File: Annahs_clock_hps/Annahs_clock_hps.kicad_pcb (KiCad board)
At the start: 2 copper layers, 140 x 90 mm, 44 parts, among them J1 Conn_01x06, J2 Power_inlet_vertical, SW1 Omron_B3F_SPST, SW2 Omron_B3F_SPST, SW3 Omron_B3F_SPST, SW4 Omron_B3F_SPST, SW5 Omron_B3F_SPST, U1 DS1307_DIP-8, U2 MAX7219, U3 L7805, U4 SC56-11EWA, U5 SC56-11EWA, Y1 Crystal_16MHz, Y2 Crystal_32768Hz

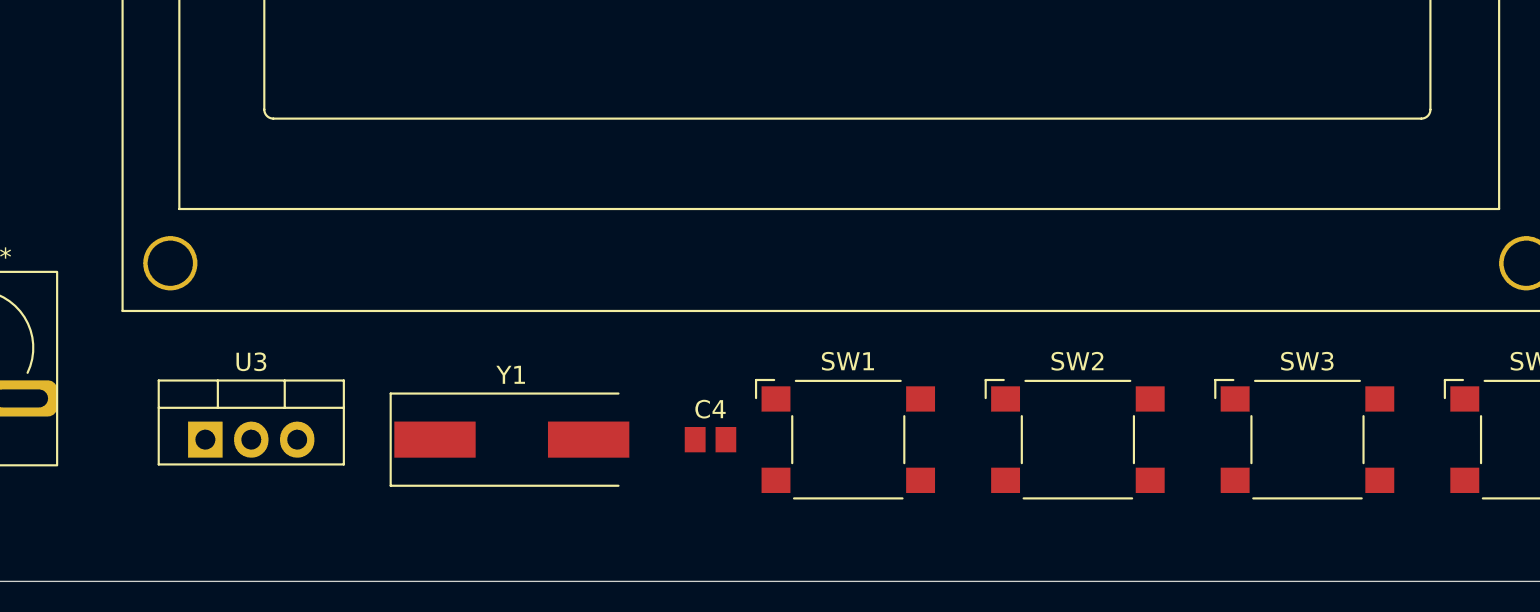
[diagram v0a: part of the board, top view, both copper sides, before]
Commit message: Updated Footprint Schematic and PCB
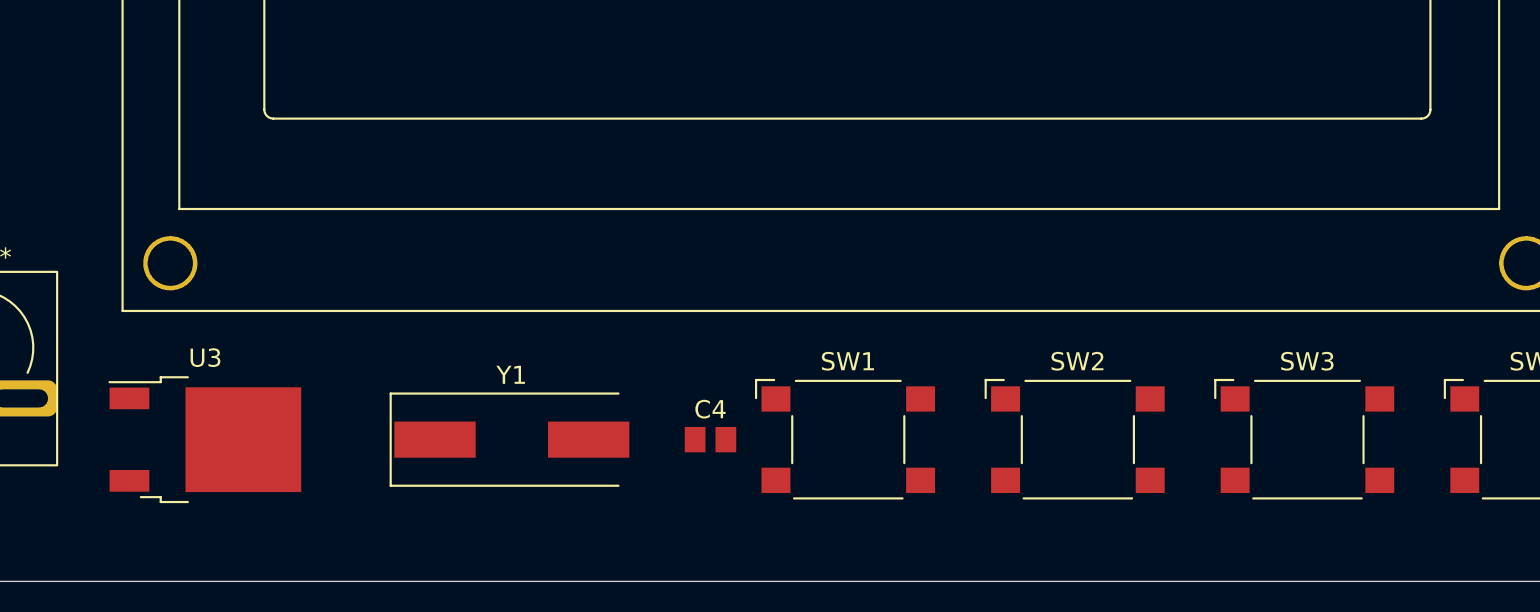
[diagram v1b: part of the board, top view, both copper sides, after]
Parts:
- U3: footprint footprints:TO-220-3_Vertical -> footprints:TO-252-2
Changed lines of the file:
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@@
     )
   )
-  (footprint "footprints:TO-220-3_Vertical" (layer "F.Cu")
+  (footprint "footprints:TO-252-2" (layer "F.Cu")
     (at 114.3 137.16)
-    (descr "TO-220-3, Vertical, RM 2.54mm, see https://www.vishay.com/docs/66542/to-220-1.pdf")
-    (tags "TO-220-3 Vertical RM 2.54mm")
-    (property "Sheetfile" "Annahs_clock_hps.kicad_sch")
-    (property "Sheetname" "")
-    (attr smd)
-    (fp_text reference "U3" (at 2.54 -4.27) (layer "F.SilkS")
-      (effects (font (size 1 1) (thickness 0.15)))
-    )
-    (fp_text value "L7805" (at 2.54 2.5) (layer "F.Fab")
-      (effects (font (size 1 1) (thickness 0.15)))
-    )
-    (fp_text user "${REFERENCE}" (at 2.54 -4.27) (layer "F.Fab")
-      (effects (font (size 1 1) (thickness 0.15)))
-    )
-    (fp_line (start -2.58 -1.76) (end 7.66 -1.76) (layer "F.SilkS") (width 0.12))
-    (fp_line (start 4.391 -3.27) (end 4.391 -1.76) (layer "F.SilkS") (width 0.12))
-    (fp_line (start 7.66 -3.27) (end 7.66 1.371) (layer "F.SilkS") (width 0.12))
-    (fp_line (start -2.58 -3.27) (end -2.58 1.371) (layer "F.SilkS") (width 0.12))
-    (fp_line (start 0.69 -3.27) (end 0.69 -1.76) (layer "F.SilkS") (width 0.12))
-    (fp_line (start -2.58 -3.27) (end 7.66 -3.27) (layer "F.SilkS") (width 0.12))
-    (fp_line (start -2.58 1.371) (end 7.66 1.371) (layer "F.SilkS") (width 0.12))
-    (fp_line (start 7.79 -3.4) (end -2.71 -3.4) (layer "F.CrtYd") (width 0.05))
-    (fp_line (start 7.79 1.51) (end 7.79 -3.4) (layer "F.CrtYd") (width 0.05))
-    (fp_line (start -2.71 -3.4) (end -2.71 1.51) (layer "F.CrtYd") (width 0.05))
-    (fp_line (start -2.71 1.51) (end 7.79 1.51) (layer "F.CrtYd") (width 0.05))
-    (fp_line (start -2.46 -1.88) (end 7.54 -1.88) (layer "F.Fab") (width 0.1))
-    (fp_line (start 7.54 1.25) (end 7.54 -3.15) (layer "F.Fab") (width 0.1))
-    (fp_line (start -2.46 1.25) (end 7.54 1.25) (layer "F.Fab") (width 0.1))
-    (fp_line (start 4.39 -3.15) (end 4.39 -1.88) (layer "F.Fab") (width 0.1))
-    (fp_line (start -2.46 -3.15) (end -2.46 1.25) (layer "F.Fab") (width 0.1))
-    (fp_line (start 7.54 -3.15) (end -2.46 -3.15) (layer "F.Fab") (width 0.1))
-    (fp_line (start 0.69 -3.15) (end 0.69 -1.88) (layer "F.Fab") (width 0.1))
-    (pad "1" thru_hole rect locked (at 0 0) (size 1.905 2) (drill 1.1) (layers *.Cu *.Mask)
+    (descr "TO-252 / DPAK SMD package, http://www.infineon.com/cms/en/product/packages/PG-TO252/PG-TO252-3-1/")
+    (tags "DPAK TO-252 DPAK-3 TO-252-3 SOT-428")
+    (property "Sheetfile" "Annahs_clock_hps.kicad_sch")
+    (property "Sheetname" "")
+    (attr smd)
+    (fp_text reference "U3" (at 0 -4.5) (layer "F.SilkS")
+      (effects (font (size 1 1) (thickness 0.15)))
+    )
+    (fp_text value "L7805" (at 0 4.5) (layer "F.Fab")
+      (effects (font (size 1 1) (thickness 0.15)))
+    )
+    (fp_text user "${REFERENCE}" (at 0 0) (layer "F.Fab")
+      (effects (font (size 1 1) (thickness 0.15)))
+    )
+    (fp_line (start -0.97 -3.45) (end -2.47 -3.45) (layer "F.SilkS") (width 0.12))
+    (fp_line (start -2.47 -3.18) (end -5.3 -3.18) (layer "F.SilkS") (width 0.12))
+    (fp_line (start -2.47 3.45) (end -2.47 3.18) (layer "F.SilkS") (width 0.12))
+    (fp_line (start -2.47 3.18) (end -3.57 3.18) (layer "F.SilkS") (width 0.12))
+    (fp_line (start -0.97 3.45) (end -2.47 3.45) (layer "F.SilkS") (width 0.12))
+    (fp_line (start -2.47 -3.45) (end -2.47 -3.18) (layer "F.SilkS") (width 0.12))
+    (fp_line (start -5.55 3.5) (end 5.55 3.5) (layer "F.CrtYd") (width 0.05))
+    (fp_line (start 5.55 -3.5) (end -5.55 -3.5) (layer "F.CrtYd") (width 0.05))
+    (fp_line (start -5.55 -3.5) (end -5.55 3.5) (layer "F.CrtYd") (width 0.05))
+    (fp_line (start 5.55 3.5) (end 5.55 -3.5) (layer "F.CrtYd") (width 0.05))
+    (fp_line (start -1.27 -3.25) (end 3.95 -3.25) (layer "F.Fab") (width 0.1))
+    (fp_line (start -4.97 -2.655) (end -4.97 -1.905) (layer "F.Fab") (width 0.1))
+    (fp_line (start -4.97 2.655) (end -2.27 2.655) (layer "F.Fab") (width 0.1))
+    (fp_line (start -1.865 -2.655) (end -4.97 -2.655) (layer "F.Fab") (width 0.1))
+    (fp_line (start 4.95 -2.7) (end 4.95 2.7) (layer "F.Fab") (width 0.1))
+    (fp_line (start 3.95 3.25) (end -2.27 3.25) (layer "F.Fab") (width 0.1))
+    (fp_line (start -2.27 3.25) (end -2.27 -2.25) (layer "F.Fab") (width 0.1))
+    (fp_line (start -2.27 -2.25) (end -1.27 -3.25) (layer "F.Fab") (width 0.1))
+    (fp_line (start 3.95 -3.25) (end 3.95 3.25) (layer "F.Fab") (width 0.1))
+    (fp_line (start 3.95 -2.7) (end 4.95 -2.7) (layer "F.Fab") (width 0.1))
+    (fp_line (start -2.27 1.905) (end -4.97 1.905) (layer "F.Fab") (width 0.1))
+    (fp_line (start -4.97 1.905) (end -4.97 2.655) (layer "F.Fab") (width 0.1))
+    (fp_line (start 4.95 2.7) (end 3.95 2.7) (layer "F.Fab") (width 0.1))
+    (fp_line (start -4.97 -1.905) (end -2.27 -1.905) (layer "F.Fab") (width 0.1))
+    (pad "" smd rect (at 0.425 -1.525) (size 3.05 2.75) (layers "F.Paste"))
+    (pad "" smd rect (at 0.425 1.525) (size 3.05 2.75) (layers "F.Paste"))
+    (pad "" smd rect (at 3.775 1.525) (size 3.05 2.75) (layers "F.Paste"))
+    (pad "" smd rect (at 3.775 -1.525) (size 3.05 2.75) (layers "F.Paste"))
+    (pad "1" smd rect (at -4.2 -2.28) (size 2.2 1.2) (layers "F.Cu" "F.Paste" "F.Mask")
       (net 10 "Net-(C6-Pad1)") (pinfunction "IN") (pintype "power_in"))
-    (pad "2" thru_hole oval locked (at 2.54 0) (size 1.905 2) (drill 1.1) (layers *.Cu *.Mask)
+    (pad "2" smd rect (at 2.1 0) (size 6.4 5.8) (layers "F.Cu" "F.Mask")
       (net 1 "GND") (pinfunction "GND") (pintype "power_in"))
-    (pad "3" thru_hole oval locked (at 5.08 0) (size 1.905 2) (drill 1.1) (layers *.Cu *.Mask)
+    (pad "3" smd rect (at -4.2 2.28) (size 2.2 1.2) (layers "F.Cu" "F.Paste" "F.Mask")
       (net 4 "VCC") (pinfunction "OUT") (pintype "power_out"))
-    (model "${HPS3DMOD}/TO-220-3_Vertical.wrl"
+    (model "${KICAD6_3DMODEL_DIR}/Package_TO_SOT_SMD.3dshapes/TO-252-2.wrl"
       (offset (xyz 0 0 0))
       (scale (xyz 1 1 1))
@@
     (fp_arc (start 0.20066 22.9997) (mid -0.153162 22.853142) (end -0.29972 22.49932) (layer "F.SilkS") (width 0.12))
     (fp_arc (start -0.29972 8.49884) (mid -0.153162 8.145018) (end 0.20066 7.99846) (layer "F.SilkS") (width 0.12))
-    (fp_arc (start 64.20104 22.49932) (mid 64.054473 22.853115) (end 63.70066 22.9997) (layer "F.SilkS") (width 0.12))
+    (fp_arc (start 64.20104 22.49932) (mid 64.054479 22.85315) (end 63.70066 22.9997) (layer "F.SilkS") (width 0.12))
     (fp_line (start -8.25 -2.75) (end -8.25 33.75) (layer "F.CrtYd") (width 0.05))
     (fp_line (start -8.25 -2.75) (end 72.25 -2.75) (layer "F.CrtYd") (width 0.05))

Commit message: PCB and Schematic Updated
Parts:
- added C10: C_0805_0.1uf, footprints:C_0805_2012Metric, F.Cu at (141.0, 134.6)
- added C11: C_0805_0.1uf, footprints:C_0805_2012Metric, F.Cu at (93.6, 134.0)
- added C12: C_0805_0.1uf, footprints:C_0805_2012Metric, F.Cu at (163.8, 134.6)
- added C13: C_0805_0.1uf, footprints:C_0805_2012Metric, F.Cu at (117.5, 135.3)
- added J3: Conn_02x03_Odd_Even, footprints:PinHeader_2x03_P2.54mm_Vertical, F.Cu at (212.7, 95.3)
- added R12: R_0805_1K, footprints:R_0805_2012Metric, F.Cu at (140.8, 139.7)
- added R13: R_0805_1K, footprints:R_0805_2012Metric, F.Cu at (92.7, 138.8)
- added R14: R_0805_1K, footprints:R_0805_2012Metric, F.Cu at (164.5, 140.3)
- added R15: R_0805_1K, footprints:R_0805_2012Metric, F.Cu at (117.3, 140.3)
- added R16: R_0805_47, footprints:R_0805_2012Metric, F.Cu at (157.1, 92.2)
- added R17: R_0805_47, footprints:R_0805_2012Metric, F.Cu at (122.8, 91.6)
- added SW6: Omron_B3F_SPST, footprints:SW_SPST_Omron_B3FS-100xP, F.Cu at (157.1, 85.2)
- J2: moved to B.Cu
- R3, R4: value R_0805_4.7K -> R_0805_47
- moved R7 118.3 mm to (90.0, 67.3), turned to 180 degrees
- moved J1 110.7 mm to (213.4, 110.5)
- moved R6 106.9 mm to (94.0, 67.3), turned to 180 degrees
- moved U1 104.1 mm to (85.1, 78.7), turned to 90 degrees
- moved C2 99.6 mm to (99.1, 96.5)
- moved Y2 99.2 mm to (86.4, 83.2)
- moved U3 92.3 mm to (206.6, 134.4)
- moved R2 92.2 mm to (109.2, 139.1), turned to 90 degrees
- moved J2 90.5 mm to (191.9, 137.8), turned to -90 degrees
- moved C8 87.7 mm to (98.4, 69.8)
- moved R9 81.7 mm to (132.7, 140.3)
- moved C4 81.0 mm to (186.7, 69.4), turned to -90 degrees
- moved Y1 80.5 mm to (186.7, 78.7), turned to 90 degrees
- moved R4 73.8 mm to (208.9, 120.7)
- moved C3 73.7 mm to (197.3, 123.2)
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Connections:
- net /Buzzer renamed MISO
- net /Driver_Din renamed MOSI
- BT1 pad 1: GND -> /VBAT
- BT1 pad 2: /VBAT -> GND
- R1 pad 1: /Down_SW -> Net-(R1-Pad1)
- R2 pad 1: /Select_SW -> Net-(R13-Pad2)
- R3 pad 1: Net-(J1-Pad4) -> TXD
- R3 pad 2: TXD -> Net-(J1-Pad4)
- R5 pad 1: RESET -> ~{RESET}
- R6 pad 2: Net-(R6-Pad2) -> VCC
- R7 pad 2: Net-(R7-Pad2) -> VCC
- R8 pad 1: /Alarm_SW -> Net-(R14-Pad2)
- R9 pad 1: /Up_SW -> Net-(R15-Pad2)
- RV1 pad 1: Net-(DS1-Pad15) -> GND
- RV1 pad 3: Net-(DS1-Pad16) -> VCC
- SW1 pad 3: /Select_SW -> Net-(R13-Pad2)
- SW1 pad 4: /Select_SW -> Net-(R13-Pad2)
- SW2 pad 3: /Down_SW -> Net-(R1-Pad1)
- SW2 pad 4: /Down_SW -> Net-(R1-Pad1)
- SW3 pad 3: /Alarm_SW -> Net-(R14-Pad2)
- SW3 pad 4: /Alarm_SW -> Net-(R14-Pad2)
- SW4 pad 3: /Up_SW -> Net-(R15-Pad2)
- SW4 pad 4: /Up_SW -> Net-(R15-Pad2)
- U1 pad 5: Net-(R6-Pad2) -> /RTC_SDA
- U1 pad 6: Net-(R7-Pad2) -> /RTC_SCL
- U2 pad 11: /Dig0_Com -> /Dig1_Com
- U2 pad 13: /Driver_Clk -> LED_SCK
- U2 pad 2: /Dig1_Com -> /Dig0_Com
- UI1 pad 1: RESET -> ~{RESET}
- UI1 pad 19: /Driver_Clk -> LED_SCK
- UI1 pad 25: LED_SCK -> unconnected-(UI1-Pad25)
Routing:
- net /RTC_SCL: track 0.00 -> 147.5 mm, vias 0 -> 2
- net /RTC_SDA: track 0.00 -> 145.8 mm, vias 0 -> 2
- net GND: track 0.00 -> 76.4 mm, vias 0 -> 5
- net Net-(DS1-Pad15): track 0.00 -> 36.0 mm, vias 0 -> 2
- net Net-(DS1-Pad3): track 0.00 -> 33.2 mm, vias 0 -> 2
- net /Clk_Crystal1: track 0.00 -> 32.1 mm
- net /VBAT: track 0.00 -> 26.4 mm
- net Net-(C6-Pad1): track 0.00 -> 18.5 mm
- net /Clk_Crystal2: track 0.00 -> 17.2 mm
- net Net-(DS1-Pad16): track 0.00 -> 16.1 mm
- net VCC: track 0.00 -> 5.16 mm
- net /RTC_XTAL2: track 0.00 -> 4.46 mm
- net /RTC_XTAL1: track 0.00 -> 4.45 mm
- net Net-(R10-Pad2): track 0.00 -> 3.59 mm
- added copper zone on B.Cu, net GND
- added copper zone on F.Cu, net VCC

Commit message: PCB Routing
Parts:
- moved R13 71.8 mm to (164.5, 139.5)
- moved C11 71.8 mm to (165.3, 134.6)
- moved R2 71.8 mm to (181.0, 139.7)
- moved SW1 71.8 mm to (173.4, 138.4)
- moved R14 69.2 mm to (95.2, 140.3)
- moved SW3 69.2 mm to (102.9, 137.8)
- moved C12 68.8 mm to (95.0, 135.3), turned to 180 degrees
- moved R8 68.6 mm to (110.5, 139.5)
- moved R17 30.3 mm to (153.0, 92.7)
- moved C13 24.8 mm to (142.2, 135.9)
- moved SW4 24.8 mm to (149.9, 138.4)
- moved R15 24.8 mm to (142.0, 141.0)
- moved R9 24.8 mm to (157.5, 141.0)
- moved C10 22.2 mm to (118.7, 135.3)
- moved R12 22.2 mm to (118.5, 140.3)
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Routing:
- net /Alarm_SW: track 0.00 -> 172.7 mm, vias 0 -> 4
- net /LCD_RS: track 0.00 -> 88.1 mm, vias 0 -> 2
- net /LCD_Enable: track 0.00 -> 85.1 mm, vias 0 -> 2
- net /LCD_Data7: track 0.00 -> 70.9 mm, vias 0 -> 2
- net /LCD_Data4: track 0.00 -> 66.8 mm, vias 0 -> 2
- net /LCD_Data5: track 0.00 -> 64.2 mm, vias 0 -> 2
- net /LCD_Data6: track 0.00 -> 61.5 mm, vias 0 -> 2
- net /Dig01_E: track 0.00 -> 50.0 mm, vias 0 -> 2
- net Net-(DS1-Pad15): track 36.0 -> 4.25 mm, vias 2 -> 0
- net Net-(R13-Pad2): track 0.00 -> 16.7 mm
- net Net-(R1-Pad1): track 0.00 -> 16.0 mm
- net /Down_SW: track 0.00 -> 15.3 mm, vias 0 -> 1
- net Net-(R14-Pad2): track 0.00 -> 14.4 mm
- net ~{RESET}: track 0.00 -> 14.0 mm
- net Net-(R15-Pad2): track 0.00 -> 13.8 mm
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
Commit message: Updated Schematic and PCB
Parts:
- removed C12: C_0805_0.1uf, footprints:C_0805_2012Metric
- added Q1: NPN_2N3904_SOT23, footprints:SOT-23, F.Cu at (189.9, 62.4)
- J2: moved to F.Cu
- R14: value R_0805_1K -> R_0805_2.2K
- moved R14 119.4 mm to (186.1, 62.9), turned to 90 degrees
- moved C2 111.9 mm to (210.8, 91.4)
- moved R11 2.33 mm to (215.9, 83.6)
- moved R3 1.27 mm to (208.9, 116.8)
- moved R1 1.06 mm to (134.2, 139.7)
- moved C11 0.53 mm to (165.3, 135.2)
- moved R13 0.53 mm to (164.5, 140.0)
- moved J2 0.40 mm to (192.3, 137.8)
- moved C10 0.20 mm to (118.5, 135.3)
- moved R12 0.20 mm to (118.3, 140.3)
- turned R5 to 180 degrees
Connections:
- net /Alarm_SW renamed /Buzzer
- BZ1 pad 1: MISO -> Net-(BZ1-Pad1)
- BZ1 pad 2: GND -> VCC
- R14 pad 2: Net-(R14-Pad2) -> Net-(Q1-Pad1)
- R16 pad 1: GND -> Net-(DS1-Pad16)
- R8 pad 1: Net-(R14-Pad2) -> MISO
- SW3 pad 3: Net-(R14-Pad2) -> MISO
- SW3 pad 4: Net-(R14-Pad2) -> MISO
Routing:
- net LED_SCK: track 0.00 -> 169.6 mm, vias 0 -> 5
- net MISO: track 0.00 -> 168.6 mm, vias 0 -> 2
- net MOSI: track 0.00 -> 148.8 mm, vias 0 -> 6
- net /Dig1_Com: track 0.00 -> 146.7 mm, vias 0 -> 6
- net /Buzzer: track 172.7 -> 28.6 mm, vias 4 -> 1
- net /Driver_Load: track 0.00 -> 142.4 mm, vias 0 -> 1
- net /Down_SW: track 15.3 -> 136.7 mm, vias 1 -> 3
- net /Up_SW: track 5.17 -> 111.9 mm, vias 0 -> 3
- net /Dig01_A: track 0.00 -> 98.2 mm, vias 0 -> 6
- net GND: track 76.4 -> 173.2 mm, vias 5 -> 18
- net ~{RESET}: track 14.0 -> 110.7 mm, vias 0 -> 2
- net /Dig01_G: track 0.00 -> 95.6 mm, vias 0 -> 4
- net /Dig01_B: track 0.00 -> 93.5 mm, vias 0 -> 4
- net /Dig01_C: track 0.00 -> 87.1 mm, vias 0 -> 6
- net /Dig01_D: track 0.00 -> 82.3 mm, vias 0 -> 6
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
